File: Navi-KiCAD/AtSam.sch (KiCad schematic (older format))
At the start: 42 parts, among them U12 ATSAME70Q21A-AN, Y1 9HT11-32.768KDZB-T, Y2 7V-16.000MAHJ-T

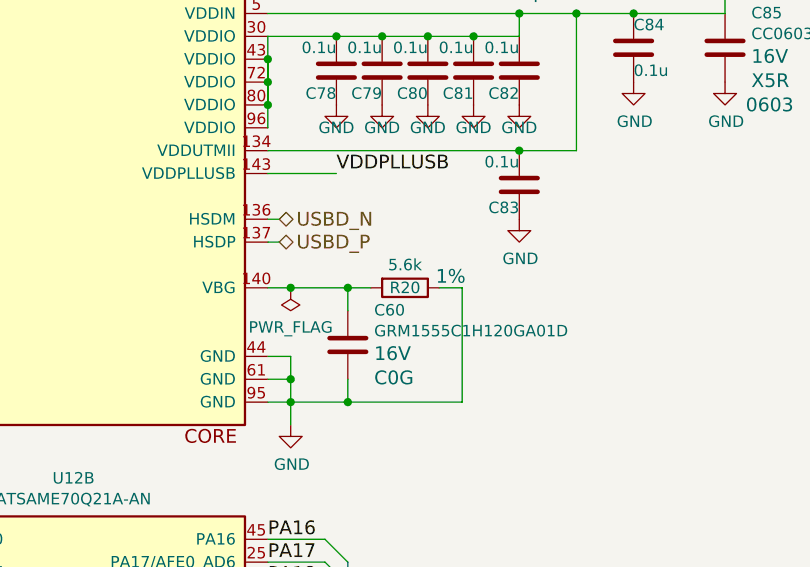
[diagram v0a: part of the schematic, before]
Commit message: Some BOM consolidation.
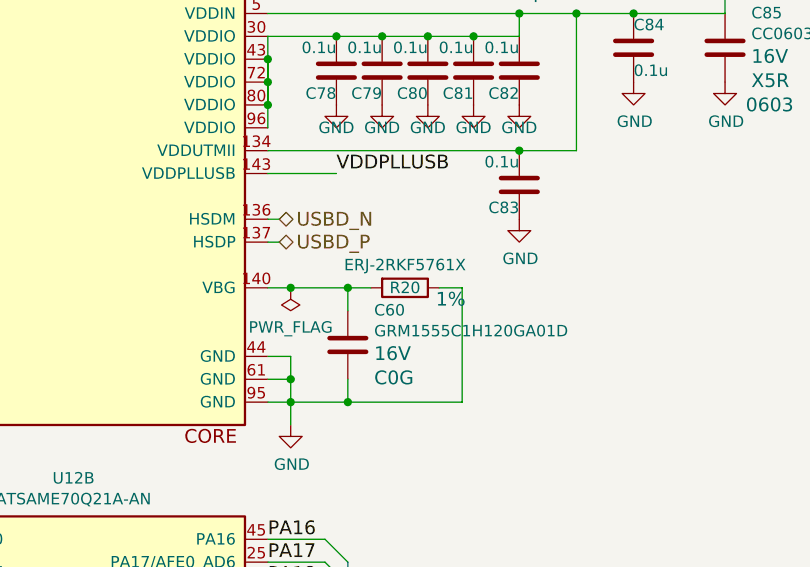
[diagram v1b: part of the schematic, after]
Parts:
- R20: value 5.6k -> ERJ-2RKF5761X
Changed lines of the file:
@@
 P 4800 2200
 F 0 "R20" V 4800 2200 50  0000 C CNN
-F 1 "5.6k" V 4700 2200 50  0000 C CNN
+F 1 "ERJ-2RKF5761X" V 4700 2200 50  0000 C CNN
 F 2 "Resistors_SMD:R_0402" V -500 400 50  0001 C CNN
 F 3 "" V -220 400 50  0001 C CNN
-F 4 "1%" V 4750 2400 60  0000 C CNN "Tolerance"
+F 4 "1%" V 4850 2400 60  0000 C CNN "Tolerance"
 F 5 "16V" V -50 400 60  0001 C CNN "Voltage"
 F 6 "0.062W" V 50  400 60  0001 C CNN "Power"

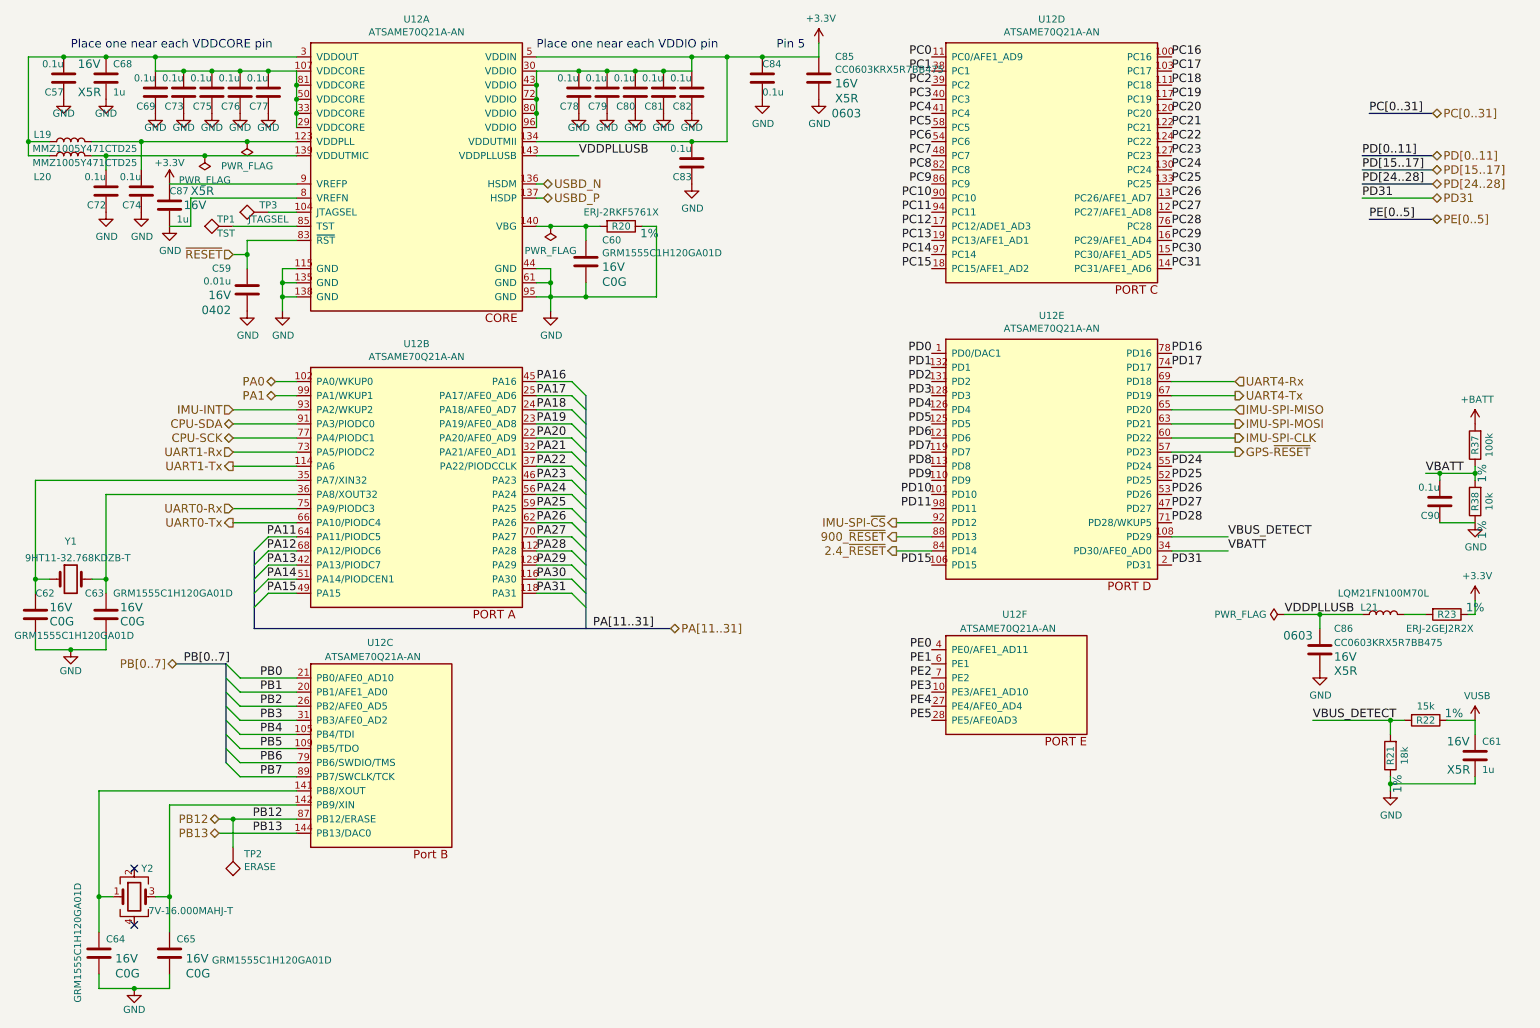
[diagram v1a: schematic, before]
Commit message: Completed key routing.
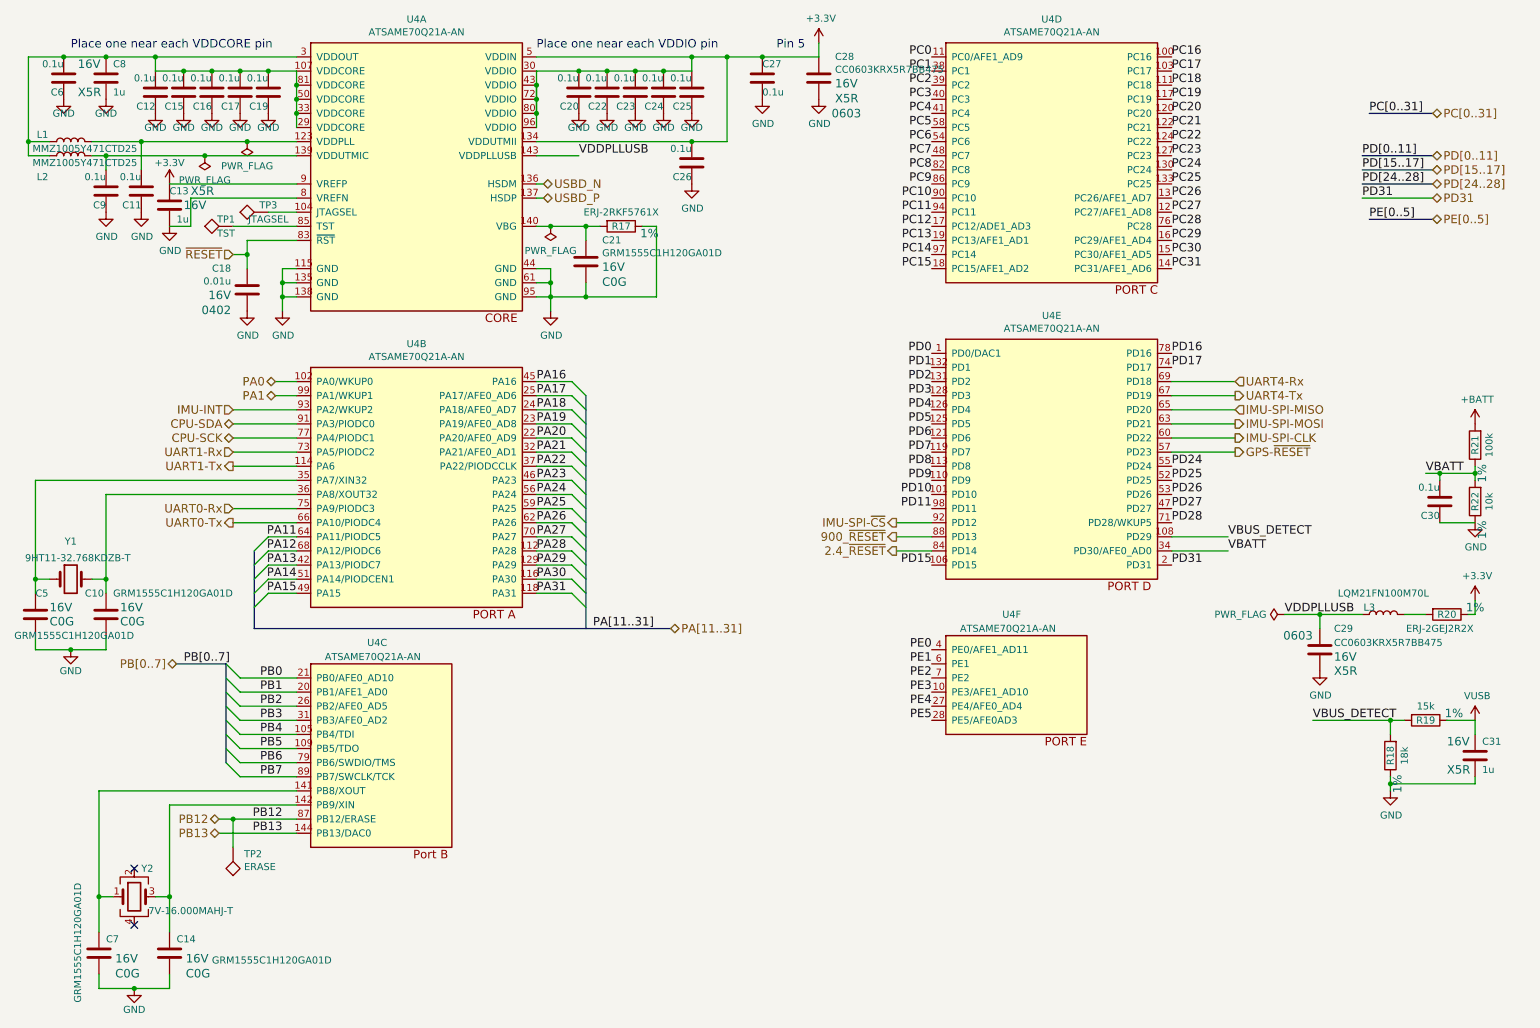
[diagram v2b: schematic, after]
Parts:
- renumbered C63 to C10, C74 to C11, C69 to C12, C87 to C13, C65 to C14, C73 to C15, C75 to C16, C76 to C17, C59 to C18, C77 to C19, C78 to C20, C60 to C21, C79 to C22, C80 to C23, C81 to C24, C82 to C25, C83 to C26, C84 to C27, C85 to C28, C86 to C29, C90 to C30, C61 to C31, C62 to C5, C57 to C6, C64 to C7, C68 to C8, C72 to C9, L19 to L1, L20 to L2, L21 to L3, R20 to R17, R21 to R18, R22 to R19, R23 to R20, R37 to R21, R38 to R22, U12 to U4

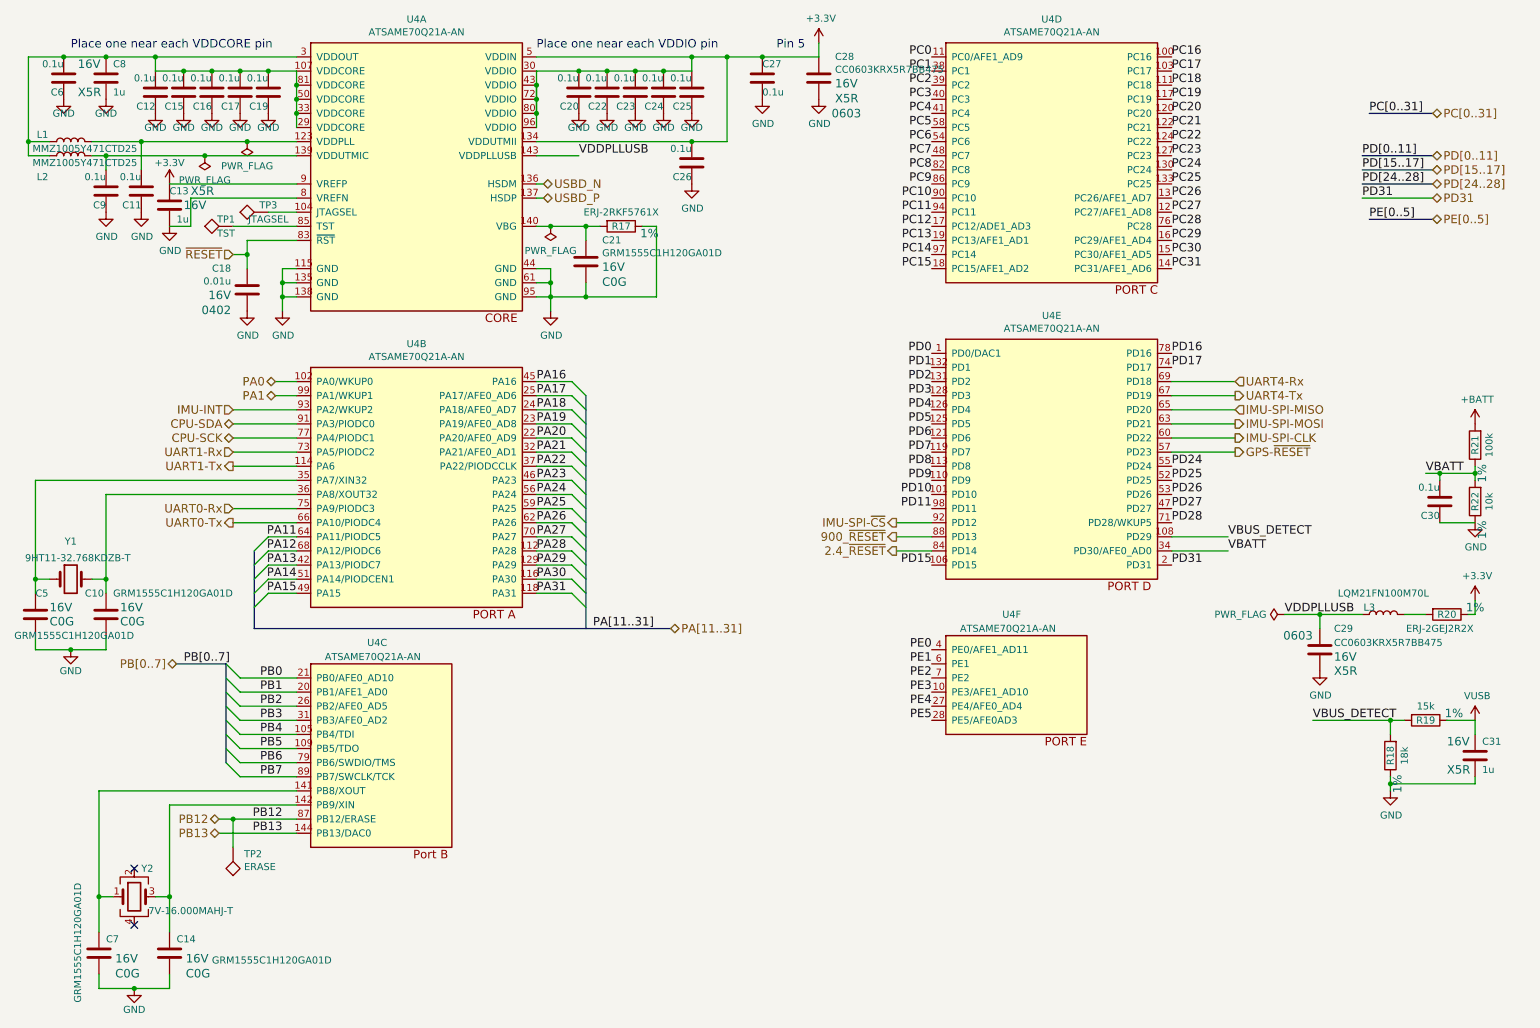
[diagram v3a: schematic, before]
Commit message: Upgraded to 9 channel RGB driver. Broke out signals for LSM303 and LSM6DS3
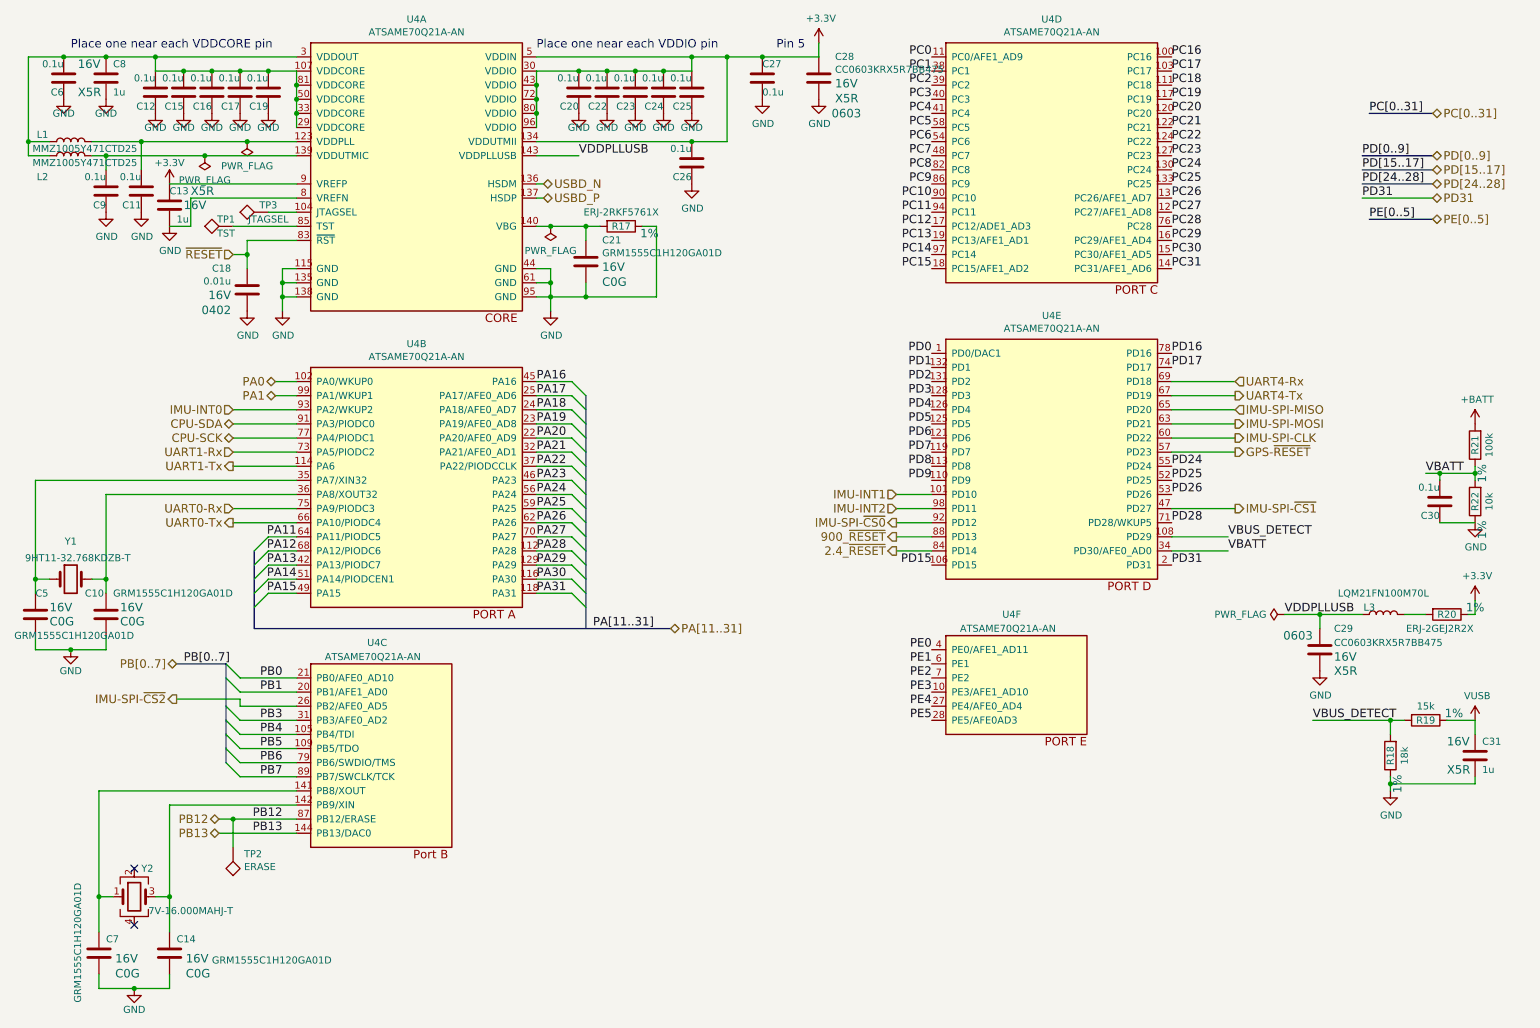
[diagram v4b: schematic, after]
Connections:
- net IMU-INT renamed IMU-INT0
- net IMU-SPI-~CS renamed IMU-SPI-~CS0
- net PB2 renamed IMU-SPI-~CS2
- net PD10 renamed IMU-INT1
- net PD11 renamed IMU-INT2
- net PD27 renamed IMU-SPI-~CS1
